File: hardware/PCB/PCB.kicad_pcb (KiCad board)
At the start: 2 copper layers, 193 x 139 mm, 13 parts, among them J1 Conn_01x02, J10 Conn_01x06_Socket, J11 Conn_01x03_Socket, J12 Conn_01x03_Socket, J13 Conn_01x03_Socket, J2 Conn_01x04, J3 Conn_01x19, J4 Conn_01x19, J5 Conn_01x02, J6 Conn_01x02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

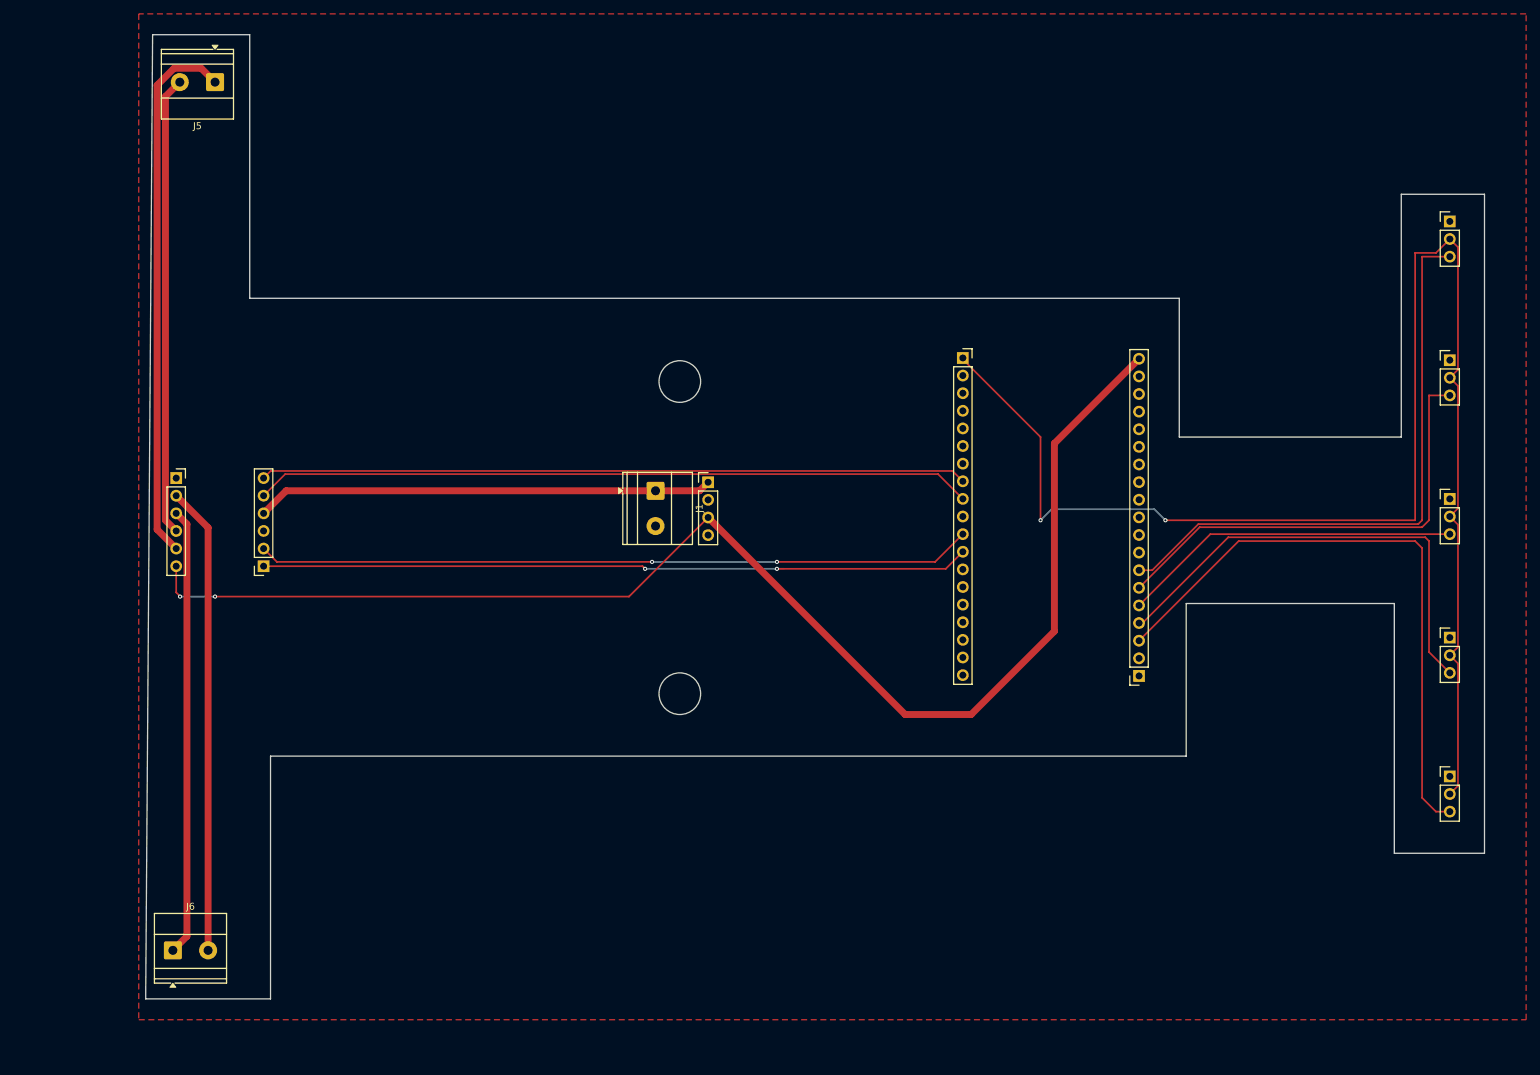
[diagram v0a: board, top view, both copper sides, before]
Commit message: Update PCB design with correct measurements.
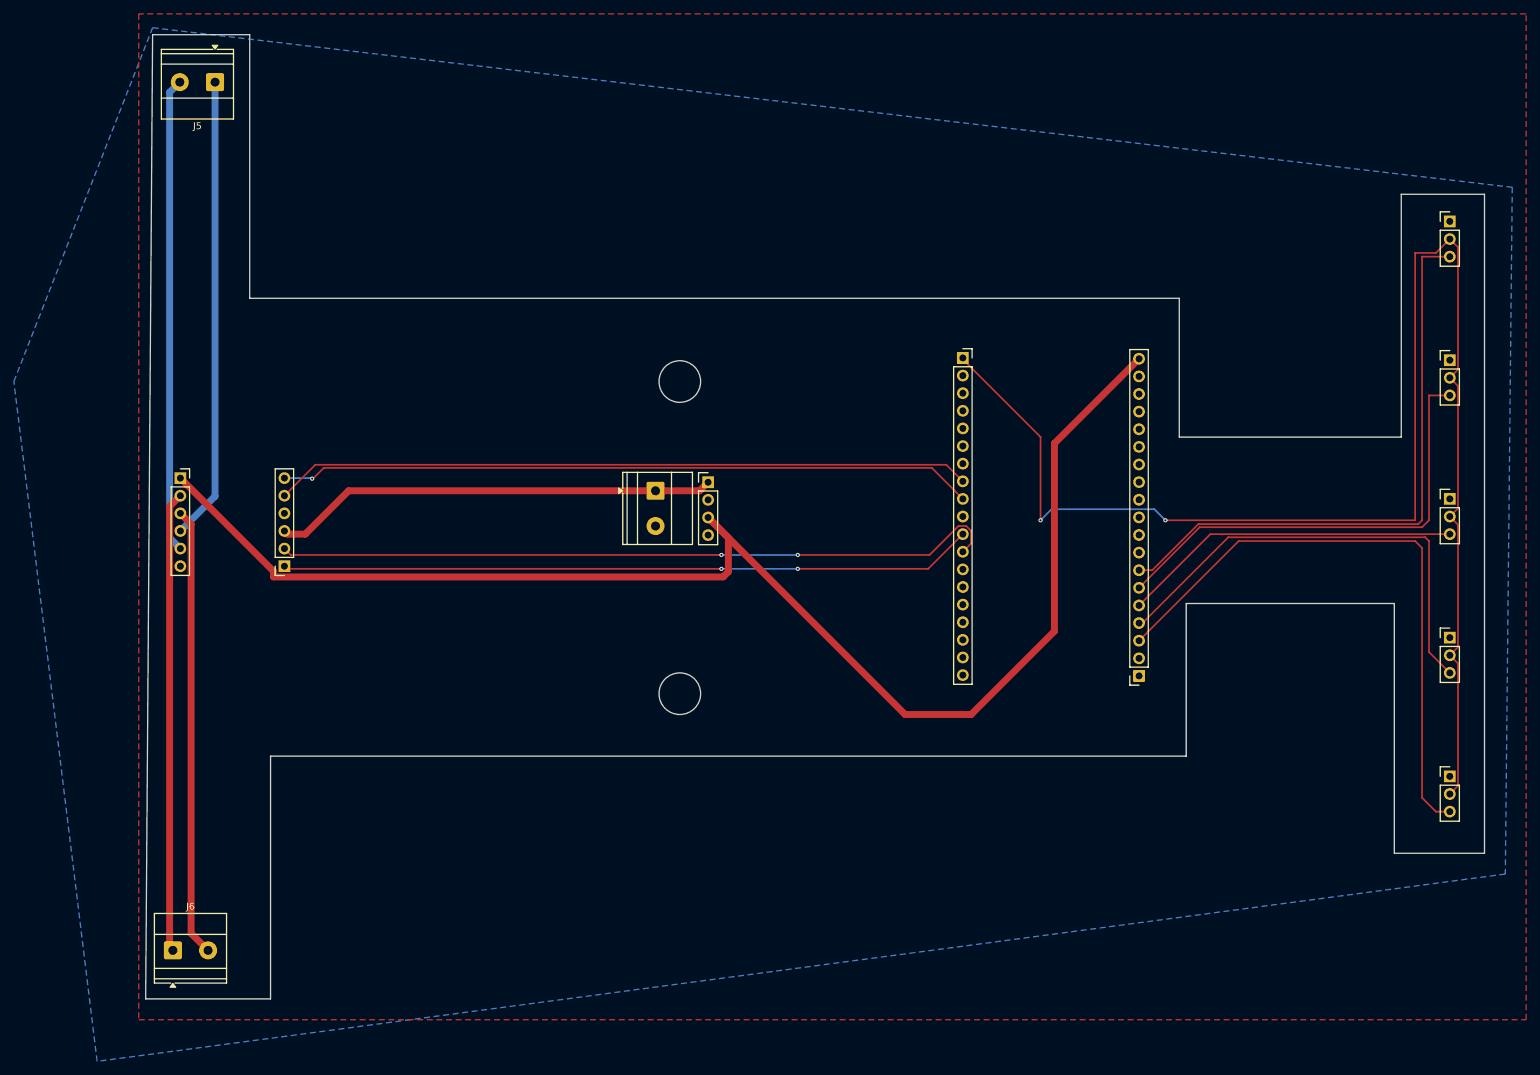
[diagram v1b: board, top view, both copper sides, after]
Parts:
- moved J9 3.00 mm to (80.0, 104.6)
- moved J10 0.60 mm to (65.0, 91.9)
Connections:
- J10 pad 1: unconnected-(J10-Pin_1-Pad1) -> +5V
- J10 pad 2: /MOT_B_2 -> /MOT_B_1
- J10 pad 3: /MOT_B_1 -> /MOT_B_2
- J10 pad 4: /MOT_A_2 -> /MOT_A_1
- J10 pad 5: /MOT_A_1 -> /MOT_A_2
- J10 pad 6: +5V -> unconnected-(J10-Pin_6-Pad6)
- J9 pad 1: /PWM_B2 -> /PWM_B1
- J9 pad 2: /PWM_B1 -> /PWM_B2
- J9 pad 3: GND -> /VBAT
- J9 pad 4: /VBAT -> GND
- J9 pad 5: /PWM_A2 -> /PWM_A1
- J9 pad 6: /PWM_A1 -> /PWM_A2
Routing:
- net /MOT_A_1: track 78.1 -> 66.8 mm
- net +5V: track 196.5 -> 205.7 mm, vias 2 -> 0
- net /PWM_A2: track 103.6 -> 100.3 mm, vias 0 -> 1
- net /PWM_B1: track 103.3 -> 100.3 mm
- net /MOT_B_2: track 67.4 -> 64.7 mm
- net /MOT_A_2: track 66.2 -> 68.5 mm
- net /PWM_B2: track 103.0 -> 104.9 mm
- net /MOT_B_1: track 64.5 -> 66.4 mm
- net /VBAT: track 65.9 -> 64.4 mm
- net /PWM_A1: track 101.8 -> 100.6 mm
- added copper zone on B.Cu, net GND
